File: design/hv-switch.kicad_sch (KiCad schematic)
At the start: 11 parts, among them Q2 GS66508B, U6 MAX22702EASA+

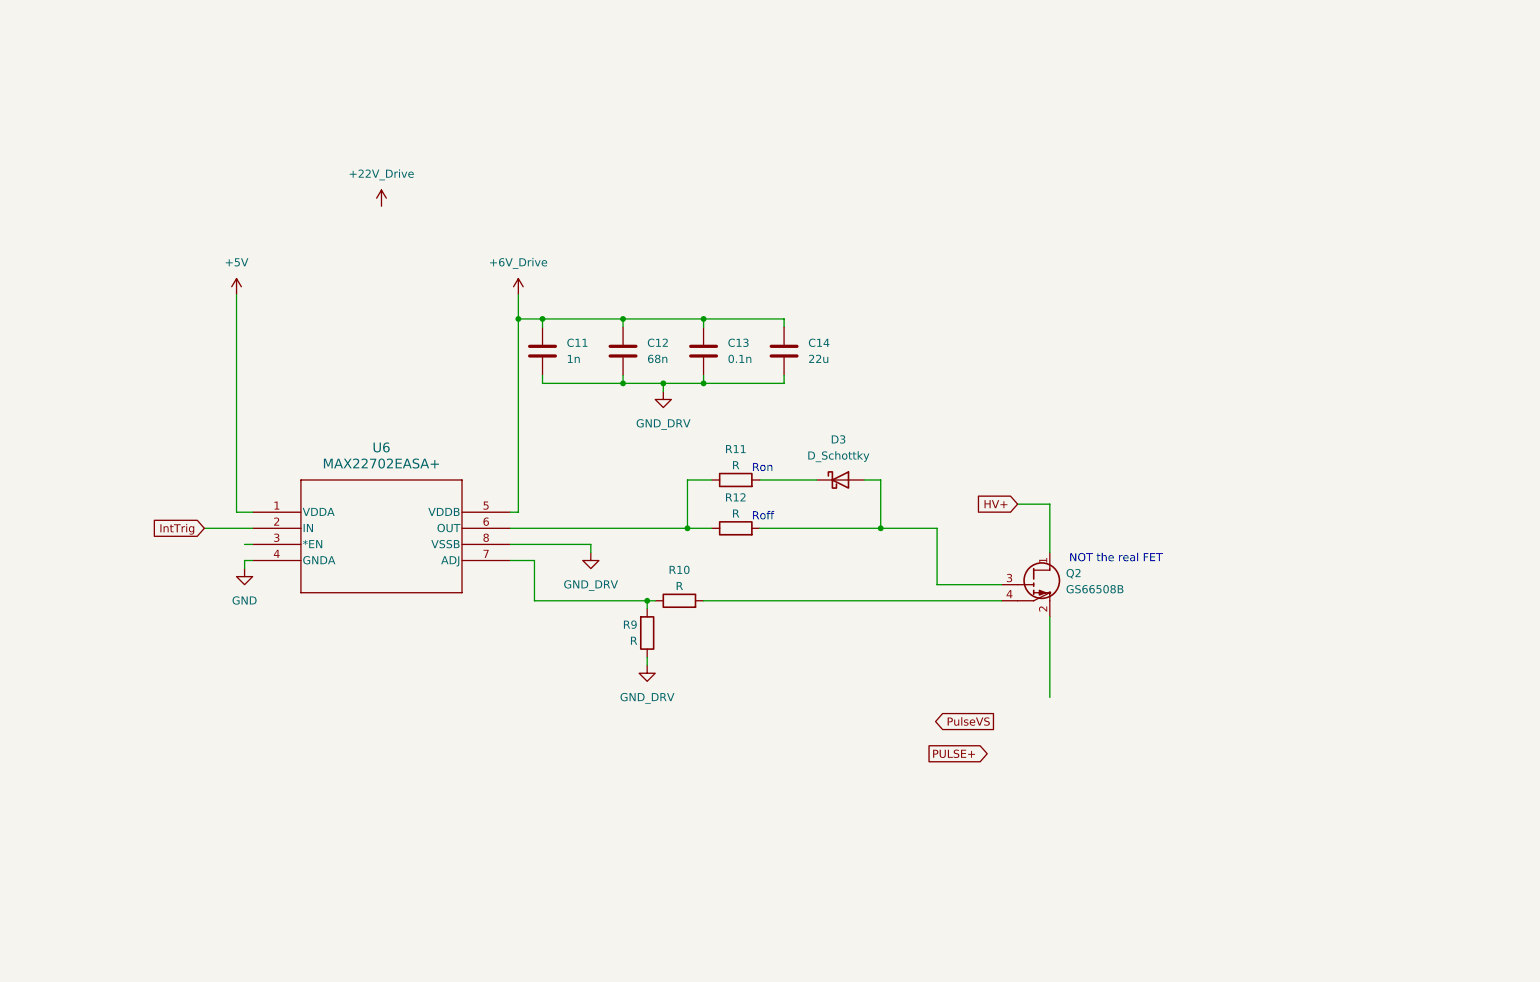
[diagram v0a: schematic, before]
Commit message: assembling final components for HV switching
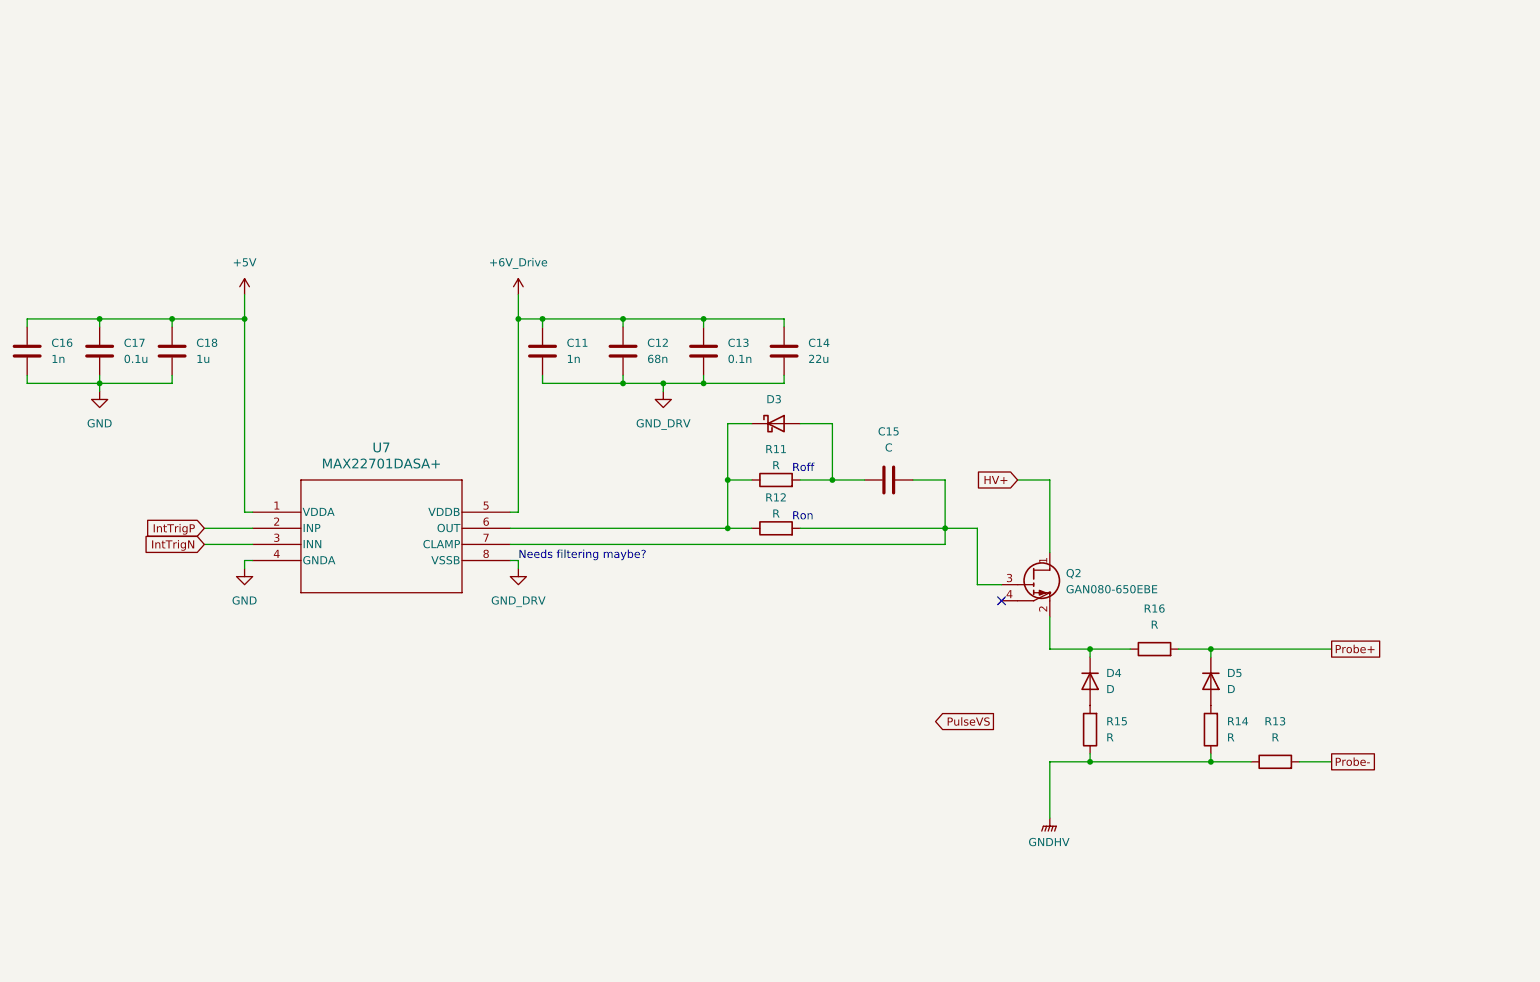
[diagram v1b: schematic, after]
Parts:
- removed R10, R9: R, symbol Device:R
- removed U6: MAX22702EASA+, 21-0041-A_8L, symbol project_symbols:MAX22702EASA+
- added C15: C, symbol Device:C
- added C16: 1n, symbol Device:C
- added C17: 0.1u, symbol Device:C
- added C18: 1u, symbol Device:C
- added D4, D5: D, symbol Device:D
- added R13, R14, R15, R16: R, symbol Device:R
- added U7: MAX22701DASA+, project-footprints:21-0041-A_8L, symbol project_symbols:MAX22701DASA+
- Q2: value GS66508B -> GAN080-650EBE; footprint Transistor_Power:GaN_Systems_GaNPX-4_7x8.4mm -> (none)
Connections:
- net +5V: now also C16.1, C17.1, C18.1, U7.1 (VDDA)
- net +6V_Drive: now also U7.5 (VDDB)
- net GND: now also C16.2, C17.2, C18.2, U7.4 (GNDA)
- net GND_DRV: now also U7.8 (VSSB)
- net at R11.1, R12.1: now also D3.1 (K), U7.6 (OUT)
- net at Q2.3 (G), R12.2: now also C15.2, U7.7 (CLAMP); no longer D3.2 (A)
- net at Q2.2 (S): now also D4.1 (K), R16.1
- net at R11.2: now also D3.2 (A), C15.1; no longer D3.1 (K)
- new net: D4.2 (A), R15.2
- new net: D5.2 (A), R14.2
- new net GNDHV: R13.1, R14.1, R15.1
- new net IntTrigN: U7.3 (INN)
- new net IntTrigP: U7.2 (INP)
- new net Probe+: D5.1 (K), R16.2
- new net Probe-: R13.2
- no-connect marks 0 -> 1
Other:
- note added: "Needs filtering maybe?"
- note removed: "NOT the real FET"
- moved on the sheet: R11, R12

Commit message: Continuing work on HV switching and primary power distribution
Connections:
- net HVSW+: now reaches D4.1 (K), Q2.2 (S), R16.1
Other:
- note removed: "Roff"
- note removed: "Ron"
- moved on the sheet: D4, D5, Q2, R13, R14, R15, R16

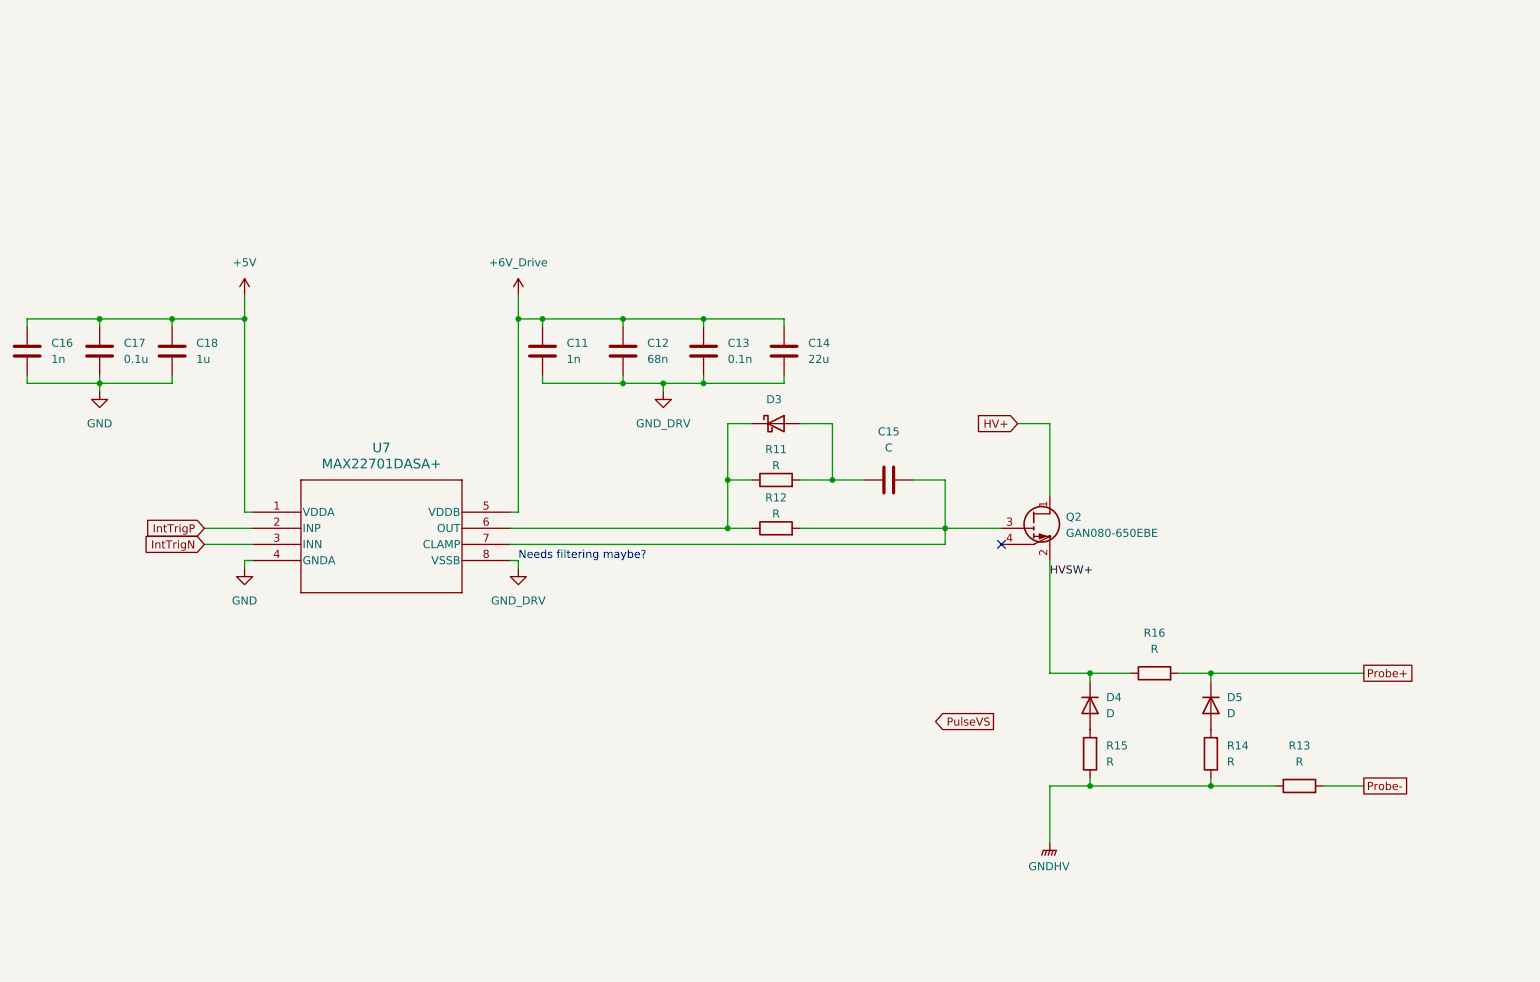
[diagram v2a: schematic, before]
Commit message: Working on probe voltage and current sense circuits
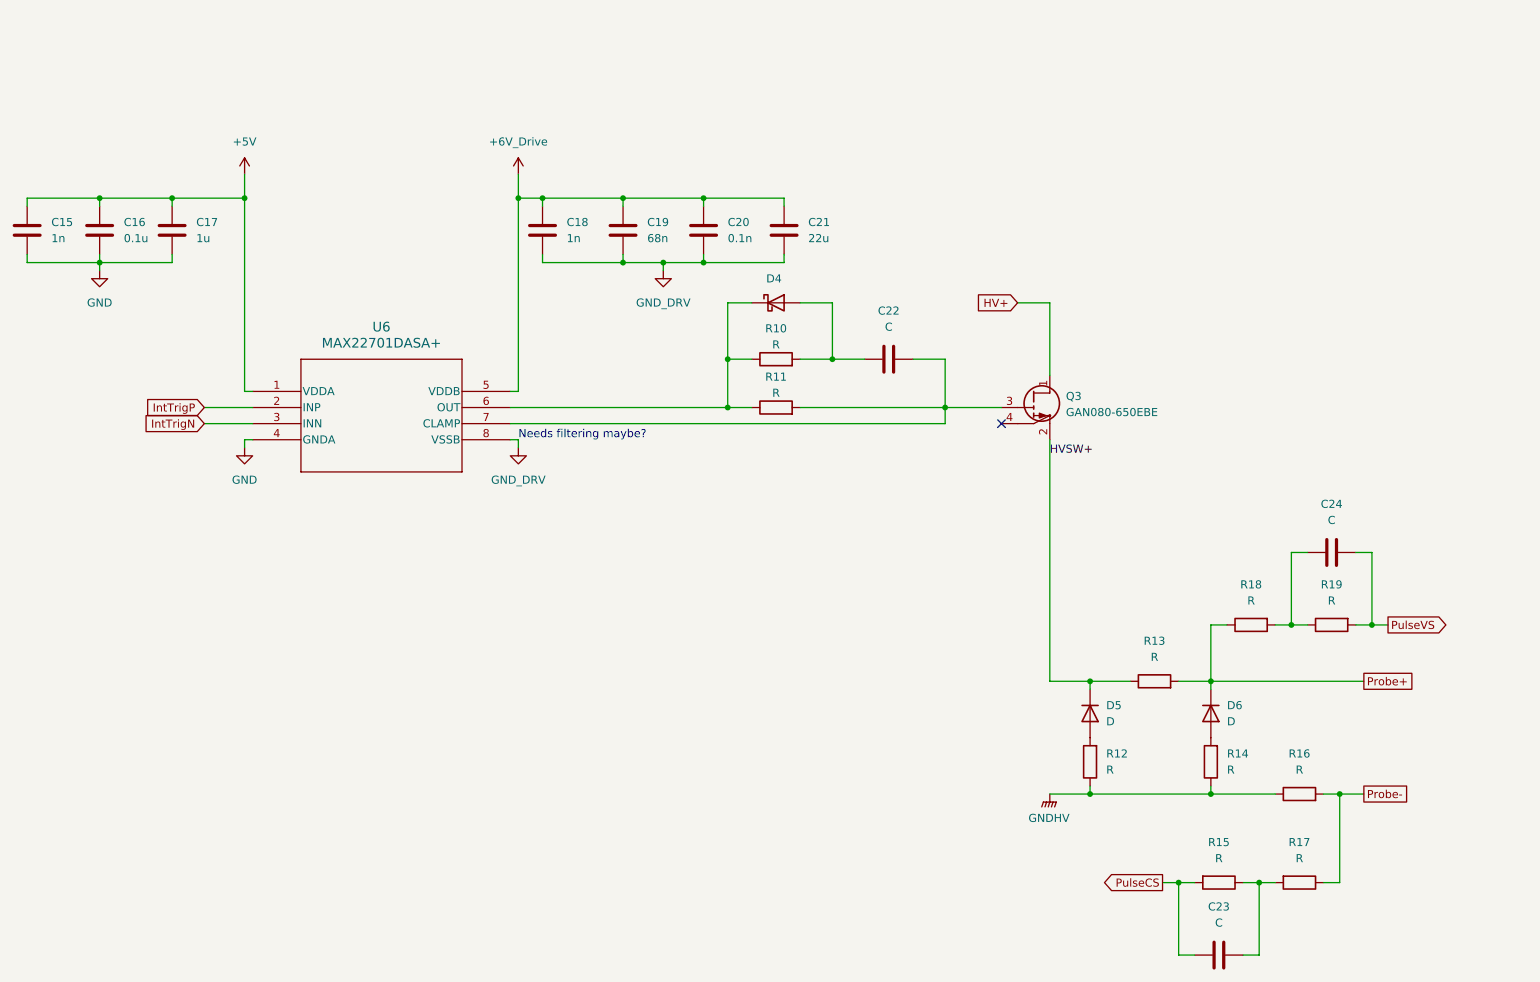
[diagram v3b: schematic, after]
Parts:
- added C23, C24: C, symbol Device:C
- added R15, R17, R18, R19: R, symbol Device:R
- renumbered C16 to C15, C17 to C16, C18 to C17, C11 to C18, C12 to C19, C13 to C20, C14 to C21, C15 to C22, D3 to D4, D4 to D5, D5 to D6, Q2 to Q3, R11 to R10, R12 to R11, R15 to R12, R16 to R13, R13 to R16, U7 to U6
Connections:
- net Probe+: now also R18.1
- net Probe-: now also R17.1
- net PulseVS: now also C24.1, R19.2
- new net: C24.2, R18.2, R19.1
- new net: C23.2, R15.1, R17.2
- new net PulseCS: C23.1, R15.2
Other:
- moved on the sheet: C15, C16, C17, C18, C19, C20, C21, C22, D4, D5, D6, Q3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

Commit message: Trying to figure out high side driver level shifting
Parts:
- added D7: D, symbol Device:D
- added R20: R, symbol Device:R
- C22: value C -> 0.1n
- R10, R11: value R -> 1
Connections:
- net HVSW+ is gone; now on net GND_DRV: D5.1 (K), Q3.2 (S), R13.1
- net +6V_Drive: now also R20.1; no longer C18.1, C19.1, C20.1, C21.1, U6.5 (VDDB)
- new net: C18.1, C19.1, C20.1, C21.1, D7.1 (K), U6.5 (VDDB)
- new net: D7.2 (A), R20.2
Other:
- note added: "If not available, this can be easily swapped for the MAX22701EASA"
- note added: "This turn on / off circuit is kind of a best guess, could use further tuning"
- note removed: "Needs filtering maybe?"

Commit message: _
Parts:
- added U7: MAX22702EASA+, 21-0041-A_8L, symbol project_symbols:MAX22702EASA+
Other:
- note added: "I think the UVLO is too high on the 01 so I might have to use the 02"
- note added: "Provides a buffer between Probe+ flybacksand the gate driver reference | V"
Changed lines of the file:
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@@
+		)
+	)
+	(text "I think the UVLO is too high \non the 01 so I might have to\nuse the 02"
+		(exclude_from_sim no)
+		(at 90.424 127.762 0)
+		(effects
+			(font
+				(size 1.27 1.27)
+			)
+		)
+	)
+	(text "Provides a buffer between \nProbe+ flybacksand the \ngate driver reference\n|\nV"
+		(exclude_from_sim no)
+		(at 212.344 105.664 0)
+		(effects
+			(font
+				(size 1.27 1.27)
+			)
 		)
 	)
@@
 					(unit 1)
 				)
+			)
+		)
+	)
+	(symbol
+		(lib_id "project_symbols:MAX22702EASA+")
+		(at 69.85 109.22 0)
+		(unit 1)
+		(exclude_from_sim no)
+		(in_bom yes)
+		(on_board yes)
+		(dnp no)
+		(fields_autoplaced yes)
+		(property "Reference" "U7"
+			(at 90.17 99.06 0)
+			(effects
+				(font
+					(size 1.524 1.524)
+				)
+			)
+		)
+		(property "Value" "MAX22702EASA+"
+			(at 90.17 101.6 0)
+			(effects
+				(font
+					(size 1.524 1.524)
+				)
+			)
+		)
+		(property "Footprint" "21-0041-A_8L"
+			(at 69.85 109.22 0)
+			(effects
+				(font
+					(size 1.27 1.27)
+					(italic yes)
+				)
+				(hide yes)
+			)
+		)
+		(property "Datasheet" "MAX22702EASA+"
+			(at 69.85 109.22 0)
+			(effects
+				(font
+					(size 1.27 1.27)
+					(italic yes)
+				)
+				(hide yes)
+			)
+		)
+		(property "Description" ""
+			(at 69.85 109.22 0)
+			(effects
+				(font
+					(size 1.27 1.27)
+				)
+				(hide yes)
+			)
+		)
+		(pin "4"
+		)
+		(pin "6"
+		)
+		(pin "8"
+		)
+		(pin "2"
+		)
+		(pin "7"
+		)
+		(pin "3"
+		)
+		(pin "5"
+		)
+		(pin "1"
+		)
+		(instances
+			(project ""
+				(path "/e1be550d-9ce6-42b1-a89a-c00b9d7586dd/a0344160-5a1e-4ade-9868-d857907b9d6d"
+					(reference "U7")
+					(unit 1)
+				)
